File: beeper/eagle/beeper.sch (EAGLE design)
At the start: 32 parts, among them J4 ICSP, Q1 16MHz, T1 MMBT3904, U1 ATA6631, U2 ATMEGA328P

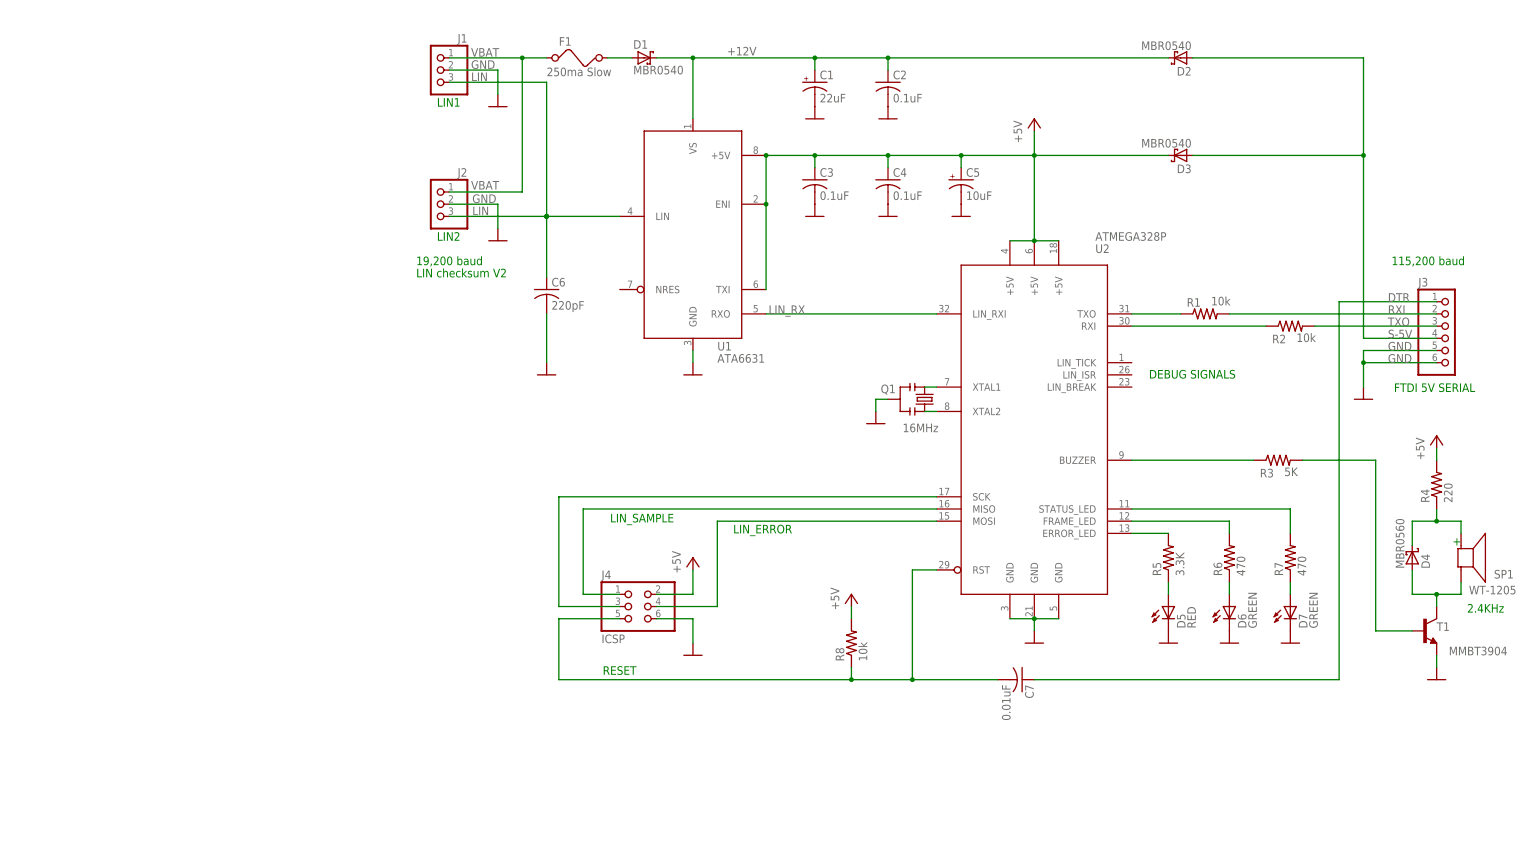
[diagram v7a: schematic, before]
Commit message: Refactoring the beeper schema. No semantic change.
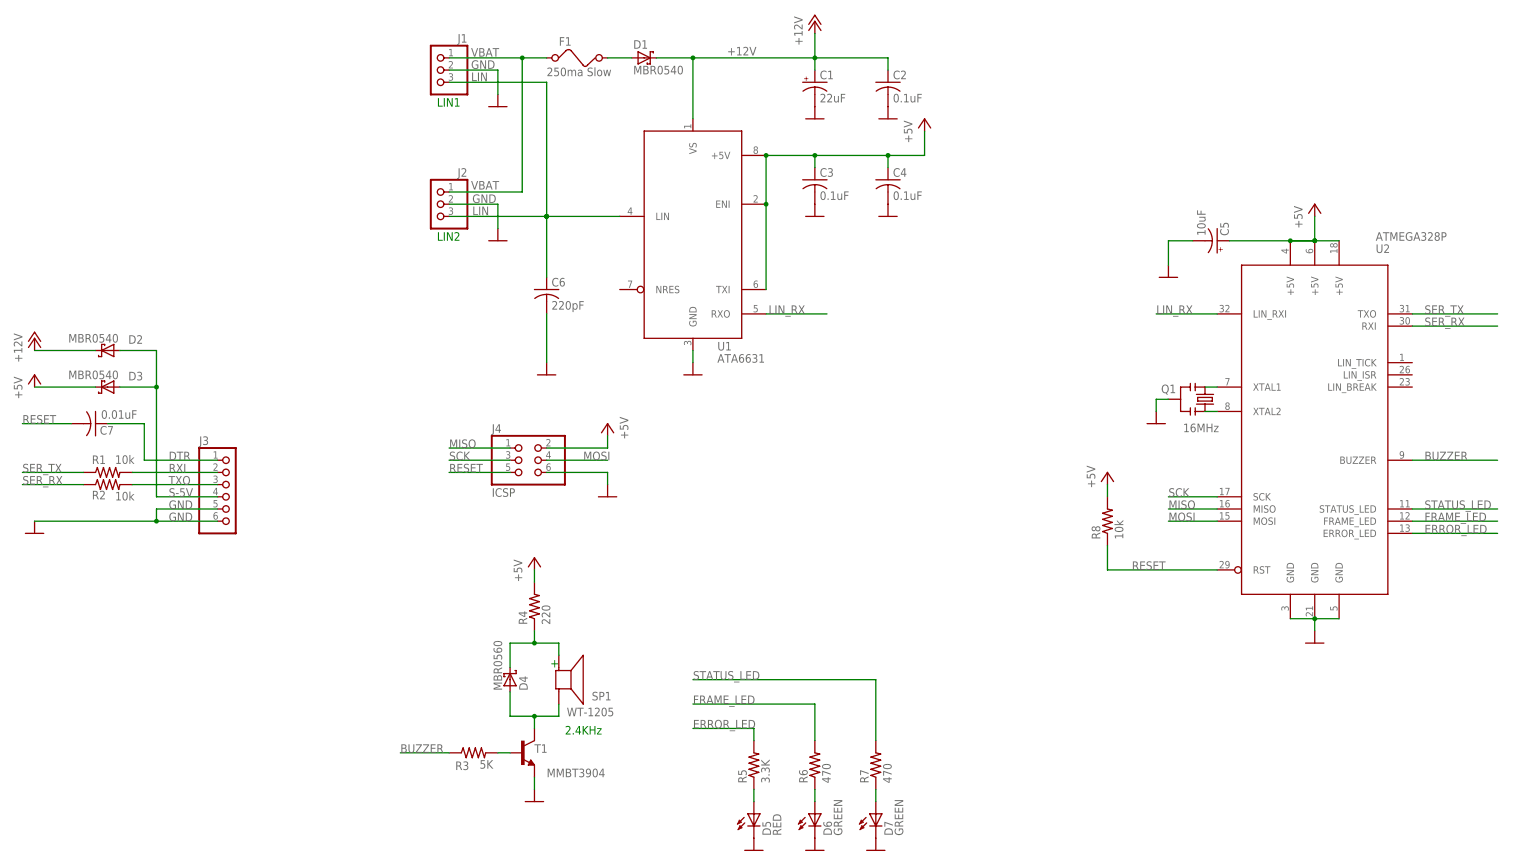
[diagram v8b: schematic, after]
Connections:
- net N$14 renamed SER_RX
- net N$15 renamed RESET
- net N$17 renamed BUZZER
- net N$20 renamed MOSI
- net N$22 renamed SER_TX
- net N$25 renamed MISO
- net N$28 renamed SCK
- net N$7 renamed ERROR_LED
- net N$8 renamed FRAME_LED
- net N$9 renamed STATUS_LED
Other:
- note removed: "115,200 baud"
- note removed: "19,200 baud"
- note removed: "DEBUG SIGNALS"
- note removed: "FTDI 5V SERIAL"
- note removed: "LIN checksum V2"
- note removed: "LIN_ERROR"
- note removed: "LIN_SAMPLE"
- note removed: "RESET"
- moved on the sheet: C5, C7, D2, D3, D4, D5, D6, D7, J3, J4, Q1, R1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
